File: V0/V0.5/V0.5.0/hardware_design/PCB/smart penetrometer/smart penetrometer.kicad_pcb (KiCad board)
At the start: 4 copper layers, 29 x 83.8 mm, 27 parts, among them J1 Conn_01x02_Female, J2 XLR3_Switched, J3 Conn_01x07_Female, J4 Screw_Terminal, U1 ADS1120-PW, U2 DS3231M, U3 4023, U4 ADS1115IDGS, U5 VO615A

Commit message: update
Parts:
- added H1: MountingHole_Pad, MountingHole:MountingHole_3.2mm_M3, F.Cu at (167.7, 56.3)
- added H2: MountingHole_Pad, MountingHole:MountingHole_3.2mm_M3, F.Cu at (186.7, 56.7)
- C6: value C_Small -> C_0.1uF
- R5, R6: value R_Small_US -> R_1kOhm
- U1: value ADS1120-PW -> ADS1120IRVAR
- U3: value 4023 -> BME260
- U4: value ADS1115IDGS -> ADS1115IRUGT
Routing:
- added copper zone on B.Cu, net GND
- added copper zone on F.Cu, net GND
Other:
- board size 29 x 83.8 mm -> 29 x 93 mm
- board text added: "SPECIES V0.5.0"
- board text removed: "SPECIES V0.4.1"

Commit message: pcb and cad update
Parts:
- added J5: Conn_02x04, Connector_PinSocket_2.54mm:PinSocket_2x04_P2.54mm_Vertical, F.Cu at (180.9, 94.1)
- H1, H2: footprint MountingHole:MountingHole_3.2mm_M3 -> MountingHole:MountingHole_3.2mm_M3_Pad
- moved R6 3.02 mm to (178.2, 98.5)
- moved H2 0.37 mm to (186.7, 56.3)
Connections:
- A1 pad 10: unconnected-(A1-D7-Pad10) -> CSN
- A1 pad 9: unconnected-(A1-D6-Pad9) -> CE
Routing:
- net MOSI: track 13.7 -> 57.8 mm
- net MISO: track 23.9 -> 65.4 mm
- net CLK: track 33.9 -> 67.2 mm
- net CSN: track 0.00 -> 27.5 mm
- net CE: track 0.00 -> 21.5 mm
- net 5V0: track 97.9 -> 99.6 mm
- net SCL: track 77.4 -> 78.4 mm

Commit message: PCB update
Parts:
- removed U4: ADS1115IRUGT, kitest:10X2QFN
- U1: footprint Package_DFN_QFN:VQFN-16-1EP_3x3mm_P0.5mm_EP1.45x1.45mm_ThermalVias -> kitest:ADS1120IPW 16TSSOP
- moved U1 18.2 mm to (182.7, 137.7), turned to 180 degrees
- moved C1 7.61 mm to (176.9, 138.2), turned to 90 degrees
- moved C2 3.17 mm to (176.8, 133.4), turned to 90 degrees
- moved R2 1.97 mm to (166.9, 138.2), turned to 90 degrees
- moved R3 1.94 mm to (174.4, 138.2), turned to -90 degrees
- moved R1 1.79 mm to (172.0, 138.2), turned to -90 degrees
- moved R4 1.73 mm to (169.3, 138.2), turned to -90 degrees
- moved R5 1.72 mm to (187.7, 94.0)
- moved C6 1.64 mm to (187.6, 81.3)
- moved C3 0.85 mm to (168.8, 133.5), turned to -90 degrees
- moved G*** 0.85 mm to (180.4, 86.1)
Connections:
- U1 pad 1: GND -> CLK
- U1 pad 10: 3V3 -> Net-(U1-AIN1)
- U1 pad 11: 3V3 -> Net-(U1-AIN0/REFP1)
- U1 pad 12: unconnected-(U1-~{DRDY}-Pad12) -> 3V3
- U1 pad 13: MISO -> 3V3
- U1 pad 14: MOSI -> unconnected-(U1-~{DRDY}-Pad14)
- U1 pad 15: CLK -> MISO
- U1 pad 16: TEMP_AMP_CS -> MOSI
- U1 pad 2: GND -> TEMP_AMP_CS
- U1 pad 4: unconnected-(U1-AIN3/REFN1-Pad4) -> GND
- U1 pad 5: unconnected-(U1-AIN2-Pad5) -> GND
- U1 pad 6: unconnected-(U1-REFN0-Pad6) -> GEO_AMP_1
- U1 pad 7: unconnected-(U1-REFP0-Pad7) -> GEO_AMP_0
- U1 pad 8: Net-(U1-AIN1) -> unconnected-(U1-REFN0-Pad8)
- U1 pad 9: Net-(U1-AIN0/REFP1) -> unconnected-(U1-REFP0-Pad9)
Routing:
- net SDA: track 74.9 -> 41.2 mm
- net SCL: track 78.4 -> 45.0 mm
- net 5V0: track 99.6 -> 68.0 mm
- net TEMP_AMP_CS: track 9.52 -> 33.4 mm, vias 1 -> 0
- net CLK: track 67.2 -> 90.0 mm, vias 1 -> 0
- net MOSI: track 57.8 -> 74.0 mm
- net Net-(U1-AIN0/REFP1): track 23.3 -> 9.14 mm
- net GEO_AMP_0: track 7.65 -> 13.7 mm
- net GEO_AMP_1: track 5.65 -> 11.0 mm
- net GND: track 12.6 -> 17.3 mm, vias 16 -> 24
- net EC_DATA: track 25.1 -> 28.4 mm
- net 3V3: track 8.35 -> 5.23 mm
- net MISO: track 65.4 -> 68.3 mm
- net TEMP_AMP_1: track 5.82 -> 7.44 mm

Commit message: PCB update
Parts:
- added C10: C_0.1uF, Capacitor_SMD:C_1206_3216Metric, B.Cu at (186.3, 133.2)
- added C7: CDIF2_100nF, Capacitor_SMD:C_1206_3216Metric, F.Cu at (177.9, 120.9)
- added C8: CCM4_10nf, Capacitor_SMD:C_1206_3216Metric, F.Cu at (178.0, 125.8)
- added C9: CCM3_10nF, Capacitor_SMD:C_1206_3216Metric, F.Cu at (177.9, 118.3)
- added R10: R_47, Resistor_SMD:R_1206_3216Metric, F.Cu at (181.7, 131.2)
- added R11: R_47, Resistor_SMD:R_1206_3216Metric, F.Cu at (188.6, 131.2)
- added R12: RF4_1K, Resistor_SMD:R_1206_3216Metric, F.Cu at (177.9, 123.3)
- added R13: RF3_1K, Resistor_SMD:R_1206_3216Metric, F.Cu at (177.9, 115.8)
- added R14: RREF_3.3K, Resistor_SMD:R_1206_3216Metric, F.Cu at (177.9, 113.2)
- added R15: RF1_1K, Resistor_SMD:R_1206_3216Metric, B.Cu at (174.4, 132.8)
- added R16: RF2_1K, Resistor_SMD:R_1206_3216Metric, B.Cu at (174.5, 130.5)
- added R17: R_1K, Resistor_SMD:R_1206_3216Metric, B.Cu at (170.7, 131.6)
- added R18: R_50, Resistor_SMD:R_1206_3216Metric, B.Cu at (174.5, 137.5)
- added R19: R_50, Resistor_SMD:R_1206_3216Metric, B.Cu at (188.3, 138.8)
- added R20: R_50, Resistor_SMD:R_1206_3216Metric, B.Cu at (188.2, 136.5)
- added R21: R_50, Resistor_SMD:R_1206_3216Metric, B.Cu at (174.5, 135.2)
- added R8: R_47, Resistor_SMD:R_1206_3216Metric, F.Cu at (186.2, 131.2)
- added R9: R_47, Resistor_SMD:R_1206_3216Metric, F.Cu at (176.9, 131.1)
- added U4: ADS1118IDGS, kitest:ADS1118_10VSSOP, B.Cu at (180.6, 133.8)
- C1: value C_0.047uF -> CCM2_10nF
- C2: value C_0.47uF -> CDIF1_100nF
- C3: value C_0.047uF -> CCM1_10nf
- R1: value R_1MOhm -> RLEAD2_3.3K
- R2: value R_1MOhm -> RLEAD1_3.3K
- R3: value R_800Ohm -> RF2_1K
- R4: value R_800Ohm -> RF1_1K
- moved R3 9.73 mm to (164.9, 136.4)
- moved R1 7.92 mm to (164.6, 141.1)
- moved C2 7.83 mm to (169.6, 136.4)
- moved C3 4.56 mm to (173.1, 134.9), turned to 0 degrees
- moved C1 3.81 mm to (173.1, 137.9), turned to 180 degrees
- moved U1 2.91 mm to (180.0, 136.6)
- moved R2 2.89 mm to (167.0, 141.1)
- moved R4 2.81 mm to (167.2, 136.4)
- moved R5 1.57 mm to (189.3, 93.9)
- moved A2 1.27 mm to (178.4, 136.0)
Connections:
- A1 pad 12: TEMP_AMP_CS -> RTD_CS
- A1 pad 8: unconnected-(A1-D5-Pad8) -> GEO_CS
- C1 pad 1: GND -> GNDA
- C3 pad 2: GND -> GNDA
- C5 pad 2: GND -> GNDA
- H2 pad 1: GND -> GNDA
- J3 pad 1: TEMP_AMP_1 -> RTD_2
- J3 pad 2: TEMP_AMP_0 -> RTD_1
- R1 pad 1: 3V3 -> Net-(R1-Pad1)
- R1 pad 2: TEMP_AMP_0 -> RTD_1
- R2 pad 1: TEMP_AMP_1 -> RTD_2
- R2 pad 2: GND -> Net-(U1-AIN3/REFN1)
- R3 pad 2: TEMP_AMP_0 -> Net-(R1-Pad1)
- R4 pad 2: TEMP_AMP_1 -> Net-(U1-AIN3/REFN1)
- U1 pad 1: CLK -> Net-(U1-SCLK)
- U1 pad 15: MISO -> Net-(U1-DOUT/~{DRDY})
- U1 pad 16: MOSI -> Net-(U1-DIN)
- U1 pad 2: TEMP_AMP_CS -> Net-(U1-~{CS})
- U1 pad 5: GND -> GNDA
- U1 pad 6: GEO_AMP_1 -> Net-(U1-AIN3/REFN1)
- U1 pad 7: GEO_AMP_0 -> unconnected-(U1-AIN2-Pad7)
- U1 pad 8: unconnected-(U1-REFN0-Pad8) -> Net-(U1-REFN0)
- U1 pad 9: unconnected-(U1-REFP0-Pad9) -> Net-(U1-REFP0)
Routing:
- net GEO_CS: track 0.00 -> 40.1 mm
- net Net-(R1-Pad1): track 0.00 -> 40.0 mm
- net GND: track 17.3 -> 51.1 mm, vias 24 -> 25
- net TEMP_AMP_CS: track 33.4 -> 0.00 mm
- net 5V0: track 68.0 -> 100.5 mm
- net Net-(U1-REFP0): track 0.00 -> 30.7 mm
- net Net-(U1-REFN0): track 0.00 -> 24.3 mm
- net Net-(U1-AIN3/REFN1): track 0.00 -> 21.0 mm
- net RTD_CS: track 0.00 -> 20.9 mm, vias 0 -> 1
- net GEO_AMP_1: track 11.0 -> 26.2 mm, vias 0 -> 1
- net Net-(U1-SCLK): track 0.00 -> 11.4 mm
- net Net-(U1-AIN1): track 25.9 -> 14.8 mm
- net VIN: track 31.2 -> 20.2 mm
- net MOSI: track 74.0 -> 84.9 mm, vias 0 -> 1
- net CLK: track 90.0 -> 100.6 mm
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- added copper zone on In1.Cu, net GNDA
- removed copper zone on In1.Cu, net GND
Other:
- board text added: "3V3"
- board text added: "DAT"

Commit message: pcb update
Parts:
- moved H2 1.10 mm to (187.8, 56.3)
- moved H1 0.90 mm to (166.8, 56.3)
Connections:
- H2 pad 1: GNDA -> GND
- J2 pad 2: VIN -> 3V3
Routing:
- net VIN: track 20.2 -> 0.00 mm
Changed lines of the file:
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@@
   )
   (footprint "MountingHole:MountingHole_3.2mm_M3_Pad" (layer "F.Cu")
-    (at 167.7 56.34)
+    (at 166.8 56.34)
     (descr "Mounting Hole 3.2mm, M3")
     (tags "mounting hole 3.2mm m3")
@@
       (net 33 "POWER") (pintype "passive"))
     (pad "2" thru_hole circle (at 0 5.08 90) (size 1.324 1.324) (drill 0.914) (layers "*.Cu" "*.Mask")
-      (net 29 "VIN") (pintype "passive"))
+      (net 17 "3V3") (pintype "passive"))
     (pad "3" thru_hole circle (at 2.032 5.08 90) (size 1.324 1.324) (drill 0.914) (layers "*.Cu" "*.Mask")
       (net 34 "unconnected-(J2-Pad3)") (pintype "passive+no_connect"))
@@
   )
   (footprint "MountingHole:MountingHole_3.2mm_M3_Pad" (layer "F.Cu")
-    (at 186.65 56.34)
+    (at 187.75 56.34)
     (descr "Mounting Hole 3.2mm, M3")
     (tags "mounting hole 3.2mm m3")
@@
       (stroke (width 0.05) (type solid)) (fill none) (layer "F.CrtYd"))
     (pad "1" thru_hole circle (at 0 0) (size 6.4 6.4) (drill 3.2) (layers "*.Cu" "*.Mask")
-      (net 37 "GNDA") (pinfunction "1") (pintype "input"))
+      (net 4 "GND") (pinfunction "1") (pintype "input"))
   )
   (footprint "Resistor_SMD:R_1206_3216Metric" (layer "F.Cu")
@@
       (net 56 "Net-(U4-AIN1)") (pinfunction "AIN1") (pintype "input"))
     (pad "6" smd roundrect (at 2.15 -1) (size 1.47 0.28) (layers "B.Cu" "B.Paste" "B.Mask") (roundrect_rratio 0.04)
-      (net 62 "unconnected-(U4-AIN2-Pad6)") (pinfunction "AIN2") (pintype "input"))
+      (net 62 "unconnected-(U4-AIN2-Pad6)") (pinfunction "AIN2") (pintype "input+no_connect"))
     (pad "7" smd roundrect (at 2.15 -0.5) (size 1.47 0.28) (layers "B.Cu" "B.Paste" "B.Mask") (roundrect_rratio 0.04)
-      (net 63 "unconnected-(U4-AIN3-Pad7)") (pinfunction "AIN3") (pintype "input"))
+      (net 63 "unconnected-(U4-AIN3-Pad7)") (pinfunction "AIN3") (pintype "input+no_connect"))
     (pad "8" smd roundrect (at 2.15 0) (size 1.47 0.28) (layers "B.Cu" "B.Paste" "B.Mask") (roundrect_rratio 0.04)
       (net 17 "3V3") (pinfunction "VDD") (pintype "power_in"))
@@
   (segment (start 188.662 73.212) (end 188.825 73.049) (width 0.6) (layer "F.Cu") (net 28))
   (segment (start 177.886 74.676) (end 172.85 69.64) (width 0.6) (layer "F.Cu") (net 28))
-  (segment (start 184.685 91.535) (end 181.258041 88.108041) (width 1) (layer "F.Cu") (net 29))
-  (segment (start 181.258041 88.108041) (end 175.195959 88.108041) (width 1) (layer "F.Cu") (net 29))
-  (segment (start 171.604 81.78) (end 170.122 81.78) (width 1) (layer "F.Cu") (net 29))
-  (segment (start 173.262 86.174082) (end 173.262 83.438) (width 1) (layer "F.Cu") (net 29))
-  (segment (start 175.195959 88.108041) (end 173.262 86.174082) (width 1) (layer "F.Cu") (net 29))
-  (segment (start 173.262 83.438) (end 171.604 81.78) (width 1) (layer "F.Cu") (net 29))
   (segment (start 165.705 136.705) (end 164.61 135.61) (width 0.25) (layer "F.Cu") (net 30))
   (segment (start 175.935 135.986396) (end 175.216396 136.705) (width 0.25) (layer "F.Cu") (net 30))

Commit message: PCB update
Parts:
- removed the C5 at (178.1, 104.1)
- removed the C7 at (177.9, 120.9)
- removed C8: CCM4_10nf, Capacitor_SMD:C_1206_3216Metric
- removed C9: CCM3_10nF, Capacitor_SMD:C_1206_3216Metric
- removed the G*** at (180.5, 76.7)
- removed the J2 at (165.0, 81.8)
- removed the R1 at (164.6, 141.1)
- removed the R10 at (181.7, 131.2)
- removed R12: RF4_1K, Resistor_SMD:R_1206_3216Metric
- removed R13: RF3_1K, Resistor_SMD:R_1206_3216Metric
- removed R14: RREF_3.3K, Resistor_SMD:R_1206_3216Metric
- removed the R2 at (167.0, 141.1)
- removed the R3 at (164.9, 136.4)
- removed the R4 at (167.2, 136.4)
- removed the R8 at (186.2, 131.2)
- removed the R9 at (176.9, 131.1)
- removed the U1 at (180.0, 136.6)
- added C6: C_1uF, Capacitor_SMD:C_1206_3216Metric, F.Cu at (165.4, 94.1)
- added G***: LOGO, kitest:qrCode, B.Cu at (177.3, 116.5)
- added J3: Conn_01x02, Connector_PinSocket_2.54mm:PinSocket_1x02_P2.54mm_Horizontal, F.Cu at (165.6, 75.7)
- added U2: ADP7157-3.3, Package_SO:SOIC-8-1EP_3.9x4.9mm_P1.27mm_EP2.29x3mm, F.Cu at (167.7, 83.6)
- C1: value CCM2_10nF -> C_10uF
- C2: value CDIF1_100nF -> C_1uF
- C3: value CCM1_10nf -> C_1uF
- C4: value C_0.1uF -> C_10uF
- G***: moved to F.Cu
- J2: renamed from J1; value Conn_01x02_Female -> Conn_01x02
- R11: value R_47 -> R_10K
- moved C2 56.3 mm to (172.8, 80.1)
- moved C3 49.9 mm to (172.8, 85.0), turned to 90 degrees
- moved C1 49.5 mm to (165.4, 89.0), turned to -90 degrees
- moved G*** 29.4 mm to (177.6, 56.8), turned to 0 degrees
- moved C4 24.6 mm to (167.4, 79.1)
- moved R11 12.8 mm to (188.8, 118.5)
- moved R3 8.95 mm to (167.4, 136.0), turned to -90 degrees
- moved R1 8.40 mm to (168.6, 139.7), turned to 180 degrees
- moved R2 5.67 mm to (169.8, 136.0), turned to -90 degrees
- moved J2 0.46 mm to (168.2, 72.3)
- renumbered C10 to C5, C6 to C7, J4 to J1, J3 to J4, R17 to R1, R6 to R10, R15 to R2, R16 to R3, R7 to R4, R18 to R5, R19 to R6, R20 to R7, R21 to R8, R5 to R9, U5 to U1, U4 to U3, U2 to U4, U3 to U5
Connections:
- A1 pad 11: 5V0 -> 3V3
- A1 pad 18: unconnected-(A1-AREF-Pad18) -> 3V3
- A1 pad 20: unconnected-(A1-A1-Pad20) -> RTD
- A1 pad 27: 5V0 -> unconnected-(A1-+5V-Pad27)
- A1 pad 30: VIN -> unconnected-(A1-VIN-Pad30)
- A1 pad 4: GND -> GNDA
- C1 pad 1: GNDA -> BATT
- C1 pad 2: Net-(U1-AIN0/REFP1) -> GND
- C2 pad 1: Net-(U1-AIN0/REFP1) -> Net-(U2-VREG)
- C2 pad 2: Net-(U1-AIN1) -> GND
- C3 pad 1: Net-(U1-AIN1) -> Net-(U2-REF)
- C3 pad 2: GNDA -> GND
- J2 pad 2: POWER -> +BATT
- J4 pad 1: RTD_2 -> 3V3
- J4 pad 2: RTD_1 -> RTD
- R11 pad 1: CLK -> RTD
- R11 pad 2: Net-(U1-SCLK) -> GNDA
- U1 pad 4: 5V0 -> 3V3
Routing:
- net 5V0: track 100.5 -> 0.00 mm
- net Net-(R1-Pad1): track 40.0 -> 0.00 mm
- net GND: track 51.1 -> 14.2 mm, vias 25 -> 31
- net RTD: track 0.00 -> 34.6 mm
- net Net-(U1-REFP0): track 30.7 -> 0.00 mm
- net BATT: track 0.00 -> 28.4 mm, vias 0 -> 1
- net Net-(U1-REFN0): track 24.3 -> 0.00 mm
- net Net-(U1-AIN3/REFN1): track 21.0 -> 0.00 mm
- net RTD_CS: track 20.9 -> 0.00 mm, vias 1 -> 0
- net Net-(U1-AIN0/REFP1): track 19.7 -> 0.00 mm
- net Net-(U1-AIN1): track 14.8 -> 0.00 mm
- net POWER: track 14.0 -> 0.00 mm
- net Net-(U1-SCLK): track 11.4 -> 0.00 mm
- net MOSI: track 84.9 -> 74.3 mm, vias 1 -> 0
- net RTD_1: track 10.3 -> 0.00 mm
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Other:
- board text added: "+"
- board text added: "BATT"
- board text added: "BY MALICHI FLEMMING II 11/25/2023"
- board text added: "SWITCH"
- board text removed: "BY MALICHI FLEMMING II 05/19/2023"
- board text removed: "OFF"
- board text removed: "ON"

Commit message: PCB update
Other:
- board text added: "SPECIES V0.5.1"
- board text removed: "SPECIES V0.5.0"
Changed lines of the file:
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@@
     (effects (font (size 0.75 0.75) (thickness 0.15)) (justify mirror))
   )
-  (gr_text "SPECIES V0.5.0" (at 177.58 58.8) (layer "B.SilkS")
+  (gr_text "SPECIES V0.5.1" (at 177.58 58.8) (layer "B.SilkS")
     (effects (font (size 1 1) (thickness 0.15)) (justify mirror))
   )

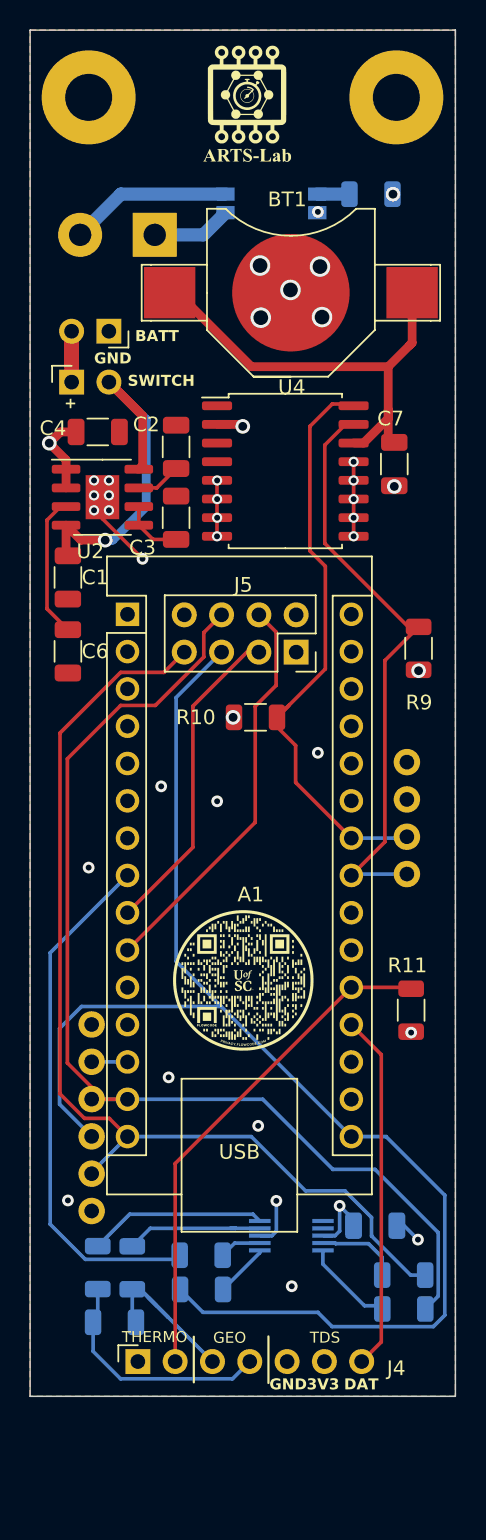
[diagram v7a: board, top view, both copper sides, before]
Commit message: reorganized folders
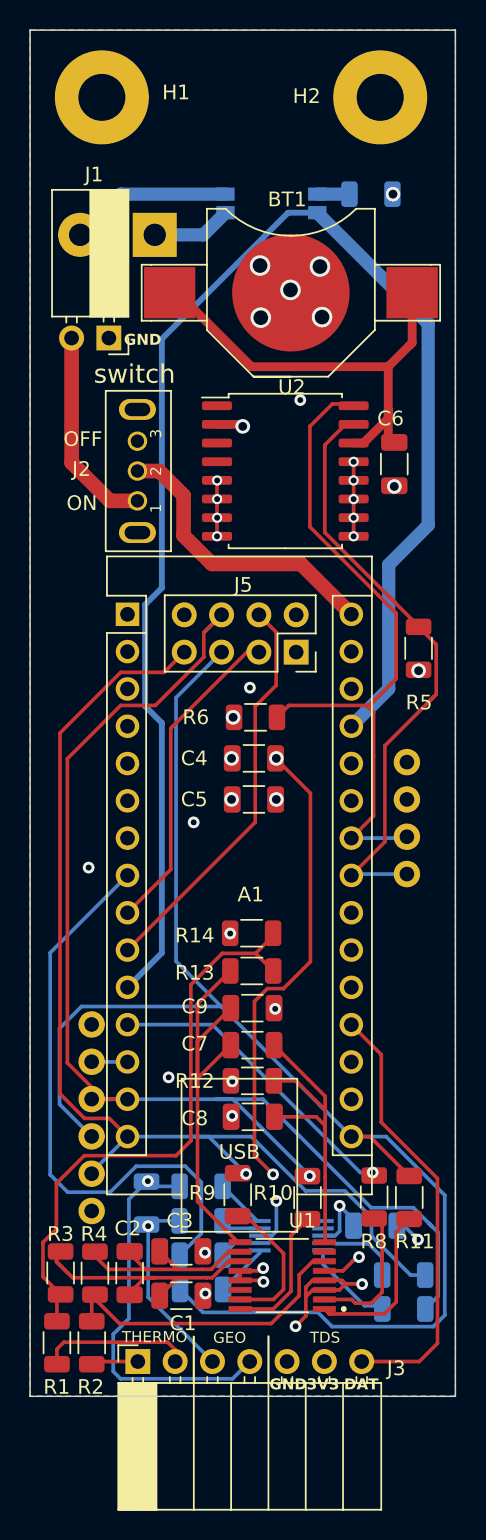
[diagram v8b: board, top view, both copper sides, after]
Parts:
- removed the C6 at (165.4, 94.1)
- removed the G*** at (177.3, 116.5)
- removed the J3 at (165.6, 75.7)
- removed the U2 at (167.7, 83.6)
- added C5: C_0.1uF, Capacitor_SMD:C_1206_3216Metric, F.Cu at (178.1, 104.1)
- added C7: CDIF2_100nF, Capacitor_SMD:C_1206_3216Metric, F.Cu at (177.9, 120.9)
- added C8: CCM4_10nf, Capacitor_SMD:C_1206_3216Metric, F.Cu at (178.0, 125.8)
- added C9: CCM3_10nF, Capacitor_SMD:C_1206_3216Metric, F.Cu at (177.9, 118.3)
- added G***: LOGO, kitest:uofsc_logo_0_75in, B.Cu at (180.5, 76.7)
- added J2: XLR3_Switched, kitest:grounded_switch, F.Cu at (165.0, 81.8)
- added R1: RLEAD2_3.3K, Resistor_SMD:R_1206_3216Metric, F.Cu at (164.6, 141.1)
- added R10: R_47, Resistor_SMD:R_1206_3216Metric, F.Cu at (181.7, 131.2)
- added R12: RF4_1K, Resistor_SMD:R_1206_3216Metric, F.Cu at (177.9, 123.3)
- added R13: RF3_1K, Resistor_SMD:R_1206_3216Metric, F.Cu at (177.9, 115.8)
- added R14: RREF_3.3K, Resistor_SMD:R_1206_3216Metric, F.Cu at (177.9, 113.2)
- added R2: RLEAD1_3.3K, Resistor_SMD:R_1206_3216Metric, F.Cu at (167.0, 141.1)
- added R3: RF2_1K, Resistor_SMD:R_1206_3216Metric, F.Cu at (164.9, 136.4)
- added R4: RF1_1K, Resistor_SMD:R_1206_3216Metric, F.Cu at (167.2, 136.4)
- added R8: R_47, Resistor_SMD:R_1206_3216Metric, F.Cu at (186.2, 131.2)
- added R9: R_47, Resistor_SMD:R_1206_3216Metric, F.Cu at (176.9, 131.1)
- added U1: ADS1120IRVAR, kitest:ADS1120IPW 16TSSOP, F.Cu at (180.0, 136.6)
- C1: value C_10uF -> CCM2_10nF
- C2: value C_1uF -> CDIF1_100nF
- C3: value C_1uF -> CCM1_10nf
- C4: value C_10uF -> C_0.1uF
- G***: moved to B.Cu
- J1: renamed from J2; value Conn_01x02 -> Conn_01x02_Female
- R11: value R_10K -> R_47
- moved C2 56.3 mm to (169.6, 136.4)
- moved C3 49.9 mm to (173.1, 134.9), turned to 0 degrees
- moved C1 49.5 mm to (173.1, 137.9), turned to 180 degrees
- moved G*** 29.4 mm to (180.4, 86.1), turned to 180 degrees
- moved C4 24.6 mm to (178.1, 101.3)
- moved R11 12.8 mm to (188.6, 131.2)
- moved R16 8.95 mm to (174.5, 130.5), turned to 180 degrees
- moved R17 8.40 mm to (170.7, 131.6), turned to 90 degrees
- moved R15 5.67 mm to (174.4, 132.8), turned to 180 degrees
- moved H2 1.10 mm to (186.7, 56.3)
- moved H1 0.90 mm to (167.7, 56.3)
- moved J1 0.46 mm to (168.2, 72.7)
- renumbered C5 to C10, C7 to C6, J4 to J3, J1 to J4, R2 to R15, R3 to R16, R1 to R17, R5 to R18, R6 to R19, R7 to R20, R8 to R21, R9 to R5, R10 to R6, R4 to R7, U4 to U2, U5 to U3, U3 to U4, U1 to U5
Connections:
- A1 pad 11: 3V3 -> 5V0
- A1 pad 18: 3V3 -> unconnected-(A1-AREF-Pad18)
- A1 pad 20: RTD -> unconnected-(A1-A1-Pad20)
- A1 pad 27: unconnected-(A1-+5V-Pad27) -> 5V0
- A1 pad 30: unconnected-(A1-VIN-Pad30) -> VIN
- A1 pad 4: GNDA -> GND
- C1 pad 1: BATT -> GNDA
- C1 pad 2: GND -> Net-(U1-AIN0/REFP1)
- C2 pad 1: Net-(U2-VREG) -> Net-(U1-AIN0/REFP1)
- C2 pad 2: GND -> Net-(U1-AIN1)
- C3 pad 1: Net-(U2-REF) -> Net-(U1-AIN1)
- C3 pad 2: GND -> GNDA
- H2 pad 1: GND -> GNDA
- J1 pad 2: +BATT -> POWER
- J3 pad 1: 3V3 -> RTD_2
- J3 pad 2: RTD -> RTD_1
- R11 pad 1: RTD -> CLK
- R11 pad 2: GNDA -> Net-(U1-SCLK)
- U5 pad 4: 3V3 -> 5V0
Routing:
- net 5V0: track 0.00 -> 100.5 mm
- net Net-(R1-Pad1): track 0.00 -> 40.0 mm
- net GND: track 14.2 -> 51.1 mm, vias 31 -> 25
- net RTD: track 34.6 -> 0.00 mm
- net Net-(U1-REFP0): track 0.00 -> 30.7 mm
- net BATT: track 28.4 -> 0.00 mm, vias 1 -> 0
- net Net-(U1-REFN0): track 0.00 -> 24.3 mm
- net Net-(U1-AIN3/REFN1): track 0.00 -> 21.0 mm
- net RTD_CS: track 0.00 -> 20.9 mm, vias 0 -> 1
- net VIN: track 0.00 -> 20.2 mm
- net Net-(U1-AIN0/REFP1): track 0.00 -> 19.7 mm
- net Net-(U1-AIN1): track 0.00 -> 14.8 mm
- net POWER: track 0.00 -> 14.0 mm
- net Net-(U1-SCLK): track 0.00 -> 11.4 mm
- net MOSI: track 74.3 -> 84.9 mm, vias 0 -> 1
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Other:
- board text added: "BY MALICHI FLEMMING II 05/19/2023"
- board text added: "OFF"
- board text added: "ON"
- board text added: "SPECIES V0.5.0"
- board text removed: "+"
- board text removed: "BATT"
- board text removed: "BY MALICHI FLEMMING II 11/25/2023"
- board text removed: "SPECIES V0.5.1"
- board text removed: "SWITCH"
